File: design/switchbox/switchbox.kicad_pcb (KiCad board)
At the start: 2 copper layers, 59.7 x 29.2 mm, 7 parts, among them J1 A0, J2 GND, SW1 SW_Push, SW2 SW_Push

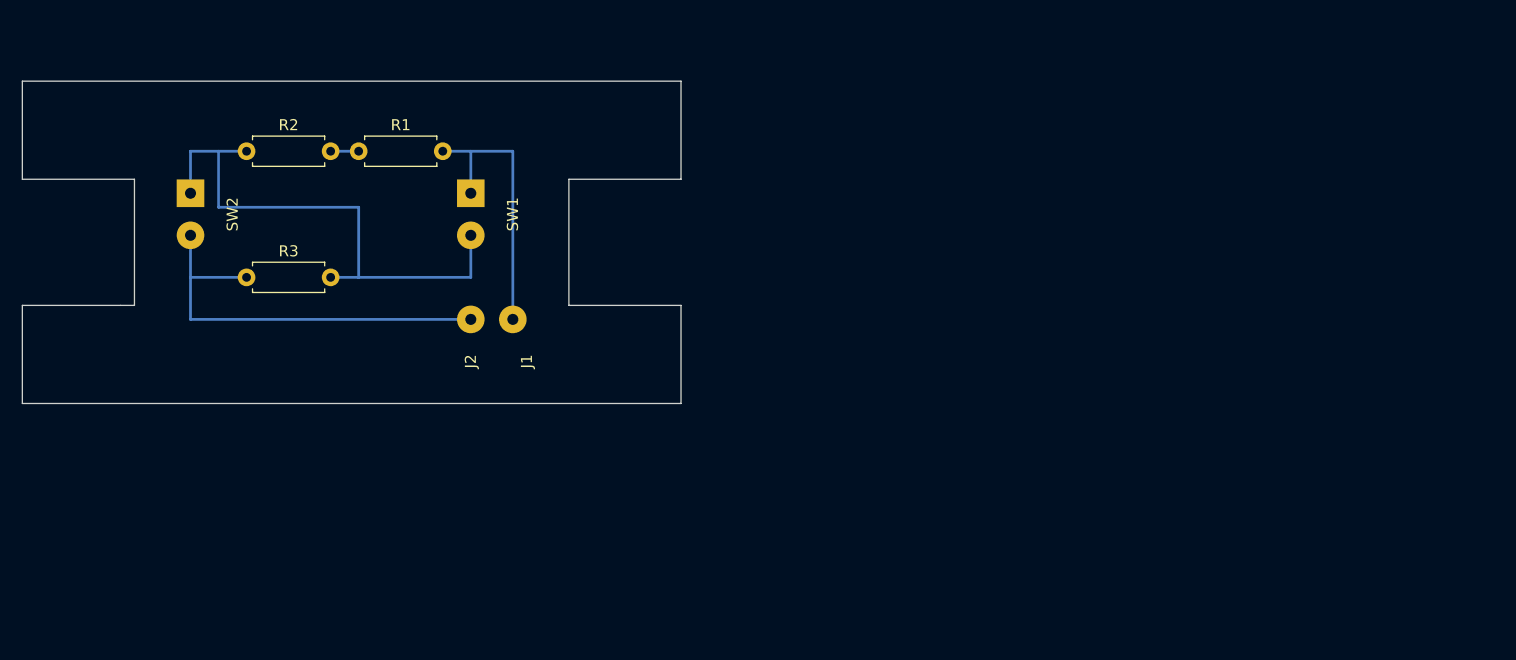
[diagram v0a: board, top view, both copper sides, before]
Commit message: Proper edge cuts alignment
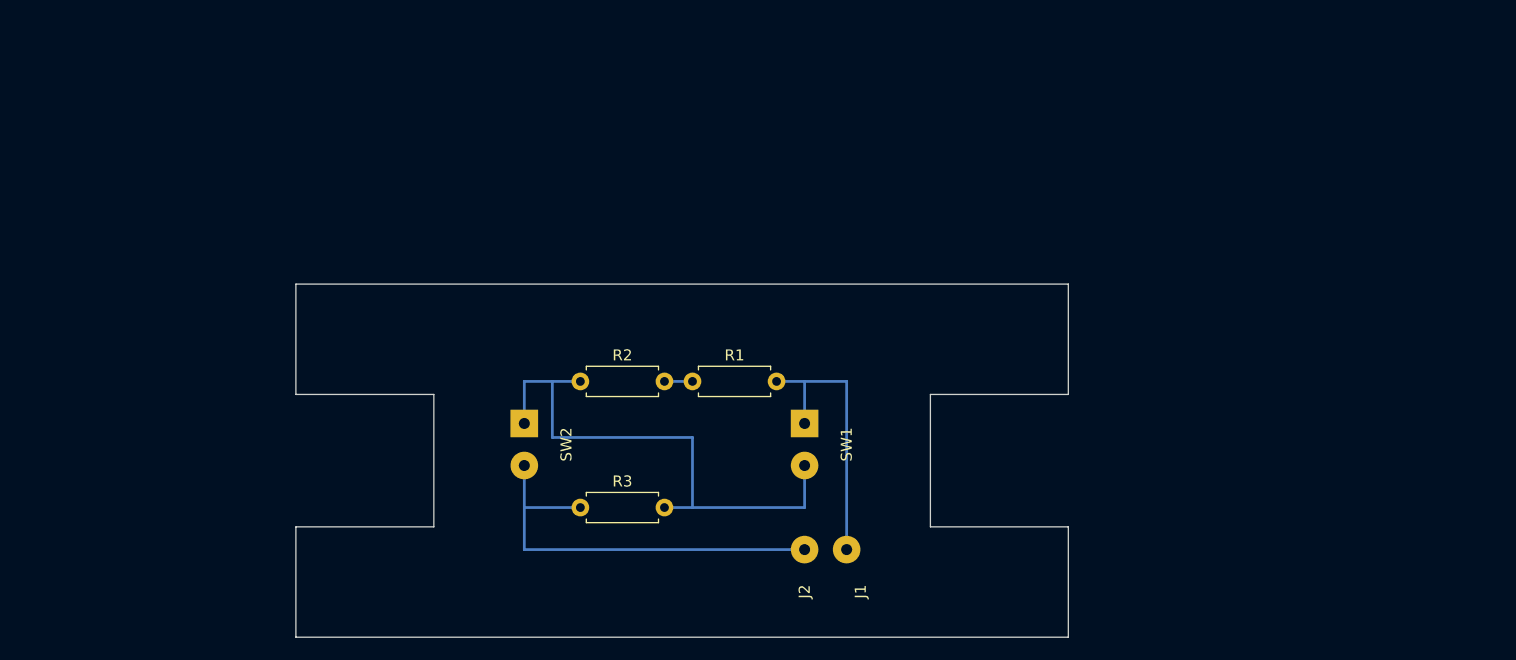
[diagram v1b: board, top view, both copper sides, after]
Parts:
- moved J1 36.7 mm to (167.4, 97.1)
- moved J2 36.7 mm to (163.6, 97.1)
- moved R1 36.7 mm to (153.4, 81.8)
- moved R2 36.7 mm to (143.3, 81.8)
- moved R3 36.7 mm to (143.3, 93.2)
- moved SW1 36.7 mm to (163.6, 85.6)
- moved SW2 36.7 mm to (138.2, 85.6)
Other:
- board size 59.7 x 29.2 mm -> 70 x 32 mm
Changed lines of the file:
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@@
-(kicad_pcb (version 20171130) (host pcbnew 5.1.4+dfsg1-1~bpo10+1)
+(kicad_pcb (version 20171130) (host pcbnew 5.1.5+dfsg1-2~bpo10+1)
   (general
     (thickness 1.6)
-    (drawings 13)
+    (drawings 12)
     (tracks 18)
     (zones 0)
@@
     (35 F.Paste user)
     (36 B.SilkS user)
-    (37 F.SilkS user)
+    (37 F.SilkS user hide)
     (38 B.Mask user)
     (39 F.Mask user)
@@
     (45 Margin user)
     (46 B.CrtYd user)
-    (47 F.CrtYd user)
+    (47 F.CrtYd user hide)
     (48 B.Fab user)
-    (49 F.Fab user)
+    (49 F.Fab user hide)
   )
   (setup
@@
       (outputformat 1)
       (mirror false)
-      (drillshape 1)
+      (drillshape 0)
       (scaleselection 1)
-      (outputdirectory ""))
+      (outputdirectory "gerber"))
   )
   (net 0 "")
@@
   )
   (module Resistor_THT:R_Axial_DIN0207_L6.3mm_D2.5mm_P7.62mm_Horizontal (layer F.Cu)
-    (at 123.19 60.96)
+    (at 153.44 81.82)
     (descr "Resistor, Axial_DIN0207 series, Axial, Horizontal, pin pitch=7.62mm, 0.25W = 1/4W, length*diameter=6.3*2.5mm^2, http://cdn-reichelt.de/documents/datenblatt/B400/1_4W%23YAG.pdf")
     (tags "Resistor Axial_DIN0207 series Axial Horizontal pin pitch 7.62mm 0.25W = 1/4W length 6.3mm diameter 2.5mm")
@@
   )
   (module Resistor_THT:R_Axial_DIN0207_L6.3mm_D2.5mm_P7.62mm_Horizontal (layer F.Cu)
-    (at 113.03 60.96)
+    (at 143.28 81.82)
     (descr "Resistor, Axial_DIN0207 series, Axial, Horizontal, pin pitch=7.62mm, 0.25W = 1/4W, length*diameter=6.3*2.5mm^2, http://cdn-reichelt.de/documents/datenblatt/B400/1_4W%23YAG.pdf")
     (tags "Resistor Axial_DIN0207 series Axial Horizontal pin pitch 7.62mm 0.25W = 1/4W length 6.3mm diameter 2.5mm")
@@
   )
   (module Resistor_THT:R_Axial_DIN0207_L6.3mm_D2.5mm_P7.62mm_Horizontal (layer F.Cu)
-    (at 113.03 72.39)
+    (at 143.28 93.25)
     (descr "Resistor, Axial_DIN0207 series, Axial, Horizontal, pin pitch=7.62mm, 0.25W = 1/4W, length*diameter=6.3*2.5mm^2, http://cdn-reichelt.de/documents/datenblatt/B400/1_4W%23YAG.pdf")
     (tags "Resistor Axial_DIN0207 series Axial Horizontal pin pitch 7.62mm 0.25W = 1/4W length 6.3mm diameter 2.5mm")
@@
   )
   (module Connector_Wire:SolderWirePad_1x02_P3.81mm_Drill1mm (layer F.Cu)
-    (at 133.35 64.77 270)
+    (at 163.6 85.63 270)
     (descr "Wire solder connection")
     (tags connector)
@@
   )
   (module Connector_Wire:SolderWirePad_1x02_P3.81mm_Drill1mm (layer F.Cu)
-    (at 107.95 64.77 270)
+    (at 138.2 85.63 270)
     (descr "Wire solder connection")
     (tags connector)
@@
   )
   (module Connector_Wire:SolderWirePad_1x01_Drill1mm (layer F.Cu)
-    (at 137.16 76.2 90)
+    (at 167.41 97.06 90)
     (descr "Wire solder connection")
     (tags connector)
@@
   )
   (module Connector_Wire:SolderWirePad_1x01_Drill1mm (layer F.Cu)
-    (at 133.35 76.2 90)
+    (at 163.6 97.06 90)
     (descr "Wire solder connection")
     (tags connector)
@@
       (net 4 GND))
   )
-  (gr_line (start 92.71 63.5) (end 92.71 54.61) (layer Edge.Cuts) (width 0.05))
-  (gr_line (start 102.87 63.5) (end 92.71 63.5) (layer Edge.Cuts) (width 0.05))
-  (gr_line (start 102.87 74.93) (end 102.87 63.5) (layer Edge.Cuts) (width 0.05))
-  (gr_line (start 101.6 74.93) (end 102.87 74.93) (layer Edge.Cuts) (width 0.05))
-  (gr_line (start 92.71 74.93) (end 101.6 74.93) (layer Edge.Cuts) (width 0.05))
-  (gr_line (start 92.71 83.82) (end 92.71 74.93) (layer Edge.Cuts) (width 0.05))
-  (gr_line (start 152.4 83.82) (end 92.71 83.82) (layer Edge.Cuts) (width 0.05))
-  (gr_line (start 152.4 74.93) (end 152.4 83.82) (layer Edge.Cuts) (width 0.05))
-  (gr_line (start 142.24 74.93) (end 152.4 74.93) (layer Edge.Cuts) (width 0.05))
-  (gr_line (start 142.24 63.5) (end 142.24 74.93) (layer Edge.Cuts) (width 0.05))
-  (gr_line (start 152.4 63.5) (end 142.24 63.5) (layer Edge.Cuts) (width 0.05))
-  (gr_line (start 152.4 54.61) (end 152.4 63.5) (layer Edge.Cuts) (width 0.05))
-  (gr_line (start 92.71 54.61) (end 152.4 54.61) (layer Edge.Cuts) (width 0.05))
-  (segment (start 120.65 60.96) (end 123.19 60.96) (width 0.25) (layer B.Cu) (net 1))
-  (segment (start 130.81 60.96) (end 133.35 60.96) (width 0.25) (layer B.Cu) (net 2))
-  (segment (start 133.35 60.96) (end 133.35 64.77) (width 0.25) (layer B.Cu) (net 2))
-  (segment (start 133.35 60.96) (end 137.16 60.96) (width 0.25) (layer B.Cu) (net 2))
-  (segment (start 137.16 60.96) (end 137.16 76.2) (width 0.25) (layer B.Cu) (net 2))
-  (segment (start 107.95 60.96) (end 107.95 64.77) (width 0.25) (layer B.Cu) (net 3))
-  (segment (start 110.49 60.96) (end 110.49 66.04) (width 0.25) (layer B.Cu) (net 3))
-  (segment (start 110.49 60.96) (end 107.95 60.96) (width 0.25) (layer B.Cu) (net 3))
-  (segment (start 113.03 60.96) (end 110.49 60.96) (width 0.25) (layer B.Cu) (net 3))
-  (segment (start 110.49 66.04) (end 123.19 66.04) (width 0.25) (layer B.Cu) (net 3))
-  (segment (start 123.19 66.04) (end 123.19 72.39) (width 0.25) (layer B.Cu) (net 3))
-  (segment (start 123.19 72.39) (end 120.65 72.39) (width 0.25) (layer B.Cu) (net 3))
-  (segment (start 123.19 72.39) (end 133.35 72.39) (width 0.25) (layer B.Cu) (net 3))
-  (segment (start 133.35 72.39) (end 133.35 68.58) (width 0.25) (layer B.Cu) (net 3))
-  (segment (start 107.95 68.58) (end 107.95 72.39) (width 0.25) (layer B.Cu) (net 4))
-  (segment (start 107.95 72.39) (end 113.03 72.39) (width 0.25) (layer B.Cu) (net 4))
-  (segment (start 107.95 72.39) (end 107.95 76.2) (width 0.25) (layer B.Cu) (net 4))
-  (segment (start 107.95 76.2) (end 133.35 76.2) (width 0.25) (layer B.Cu) (net 4))
+  (gr_line (start 187.5 105) (end 187.5 95) (layer Edge.Cuts) (width 0.05))
+  (gr_line (start 117.5 105) (end 187.5 105) (layer Edge.Cuts) (width 0.05))
+  (gr_line (start 117.5 95) (end 117.5 105) (layer Edge.Cuts) (width 0.05))
+  (gr_line (start 187.5 73) (end 187.5 83) (layer Edge.Cuts) (width 0.05))
+  (gr_line (start 117.5 73) (end 187.5 73) (layer Edge.Cuts) (width 0.05))
+  (gr_line (start 117.5 83) (end 117.5 73) (layer Edge.Cuts) (width 0.05))
+  (gr_line (start 175 95) (end 187.5 95) (layer Edge.Cuts) (width 0.05))
+  (gr_line (start 175 83) (end 187.5 83) (layer Edge.Cuts) (width 0.05))
+  (gr_line (start 130 83) (end 117.5 83) (layer Edge.Cuts) (width 0.05))
+  (gr_line (start 130 95) (end 117.5 95) (layer Edge.Cuts) (width 0.05))
+  (gr_line (start 175 95) (end 175 83) (layer Edge.Cuts) (width 0.05))
+  (gr_line (start 130 95) (end 130 83) (layer Edge.Cuts) (width 0.05))
+  (segment (start 150.9 81.82) (end 153.44 81.82) (width 0.25) (layer B.Cu) (net 1))
+  (segment (start 161.06 81.82) (end 163.6 81.82) (width 0.25) (layer B.Cu) (net 2))
+  (segment (start 163.6 81.82) (end 163.6 85.63) (width 0.25) (layer B.Cu) (net 2))
+  (segment (start 163.6 81.82) (end 167.41 81.82) (width 0.25) (layer B.Cu) (net 2))
+  (segment (start 167.41 81.82) (end 167.41 97.06) (width 0.25) (layer B.Cu) (net 2))
+  (segment (start 138.2 81.82) (end 138.2 85.63) (width 0.25) (layer B.Cu) (net 3))
+  (segment (start 140.74 81.82) (end 140.74 86.9) (width 0.25) (layer B.Cu) (net 3))
+  (segment (start 140.74 81.82) (end 138.2 81.82) (width 0.25) (layer B.Cu) (net 3))
+  (segment (start 143.28 81.82) (end 140.74 81.82) (width 0.25) (layer B.Cu) (net 3))
+  (segment (start 140.74 86.9) (end 153.44 86.9) (width 0.25) (layer B.Cu) (net 3))
+  (segment (start 153.44 86.9) (end 153.44 93.25) (width 0.25) (layer B.Cu) (net 3))
+  (segment (start 153.44 93.25) (end 150.9 93.25) (width 0.25) (layer B.Cu) (net 3))
+  (segment (start 153.44 93.25) (end 163.6 93.25) (width 0.25) (layer B.Cu) (net 3))
+  (segment (start 163.6 93.25) (end 163.6 89.44) (width 0.25) (layer B.Cu) (net 3))
+  (segment (start 138.2 89.44) (end 138.2 93.25) (width 0.25) (layer B.Cu) (net 4))
+  (segment (start 138.2 93.25) (end 143.28 93.25) (width 0.25) (layer B.Cu) (net 4))
+  (segment (start 138.2 93.25) (end 138.2 97.06) (width 0.25) (layer B.Cu) (net 4))
+  (segment (start 138.2 97.06) (end 163.6 97.06) (width 0.25) (layer B.Cu) (net 4))
 )

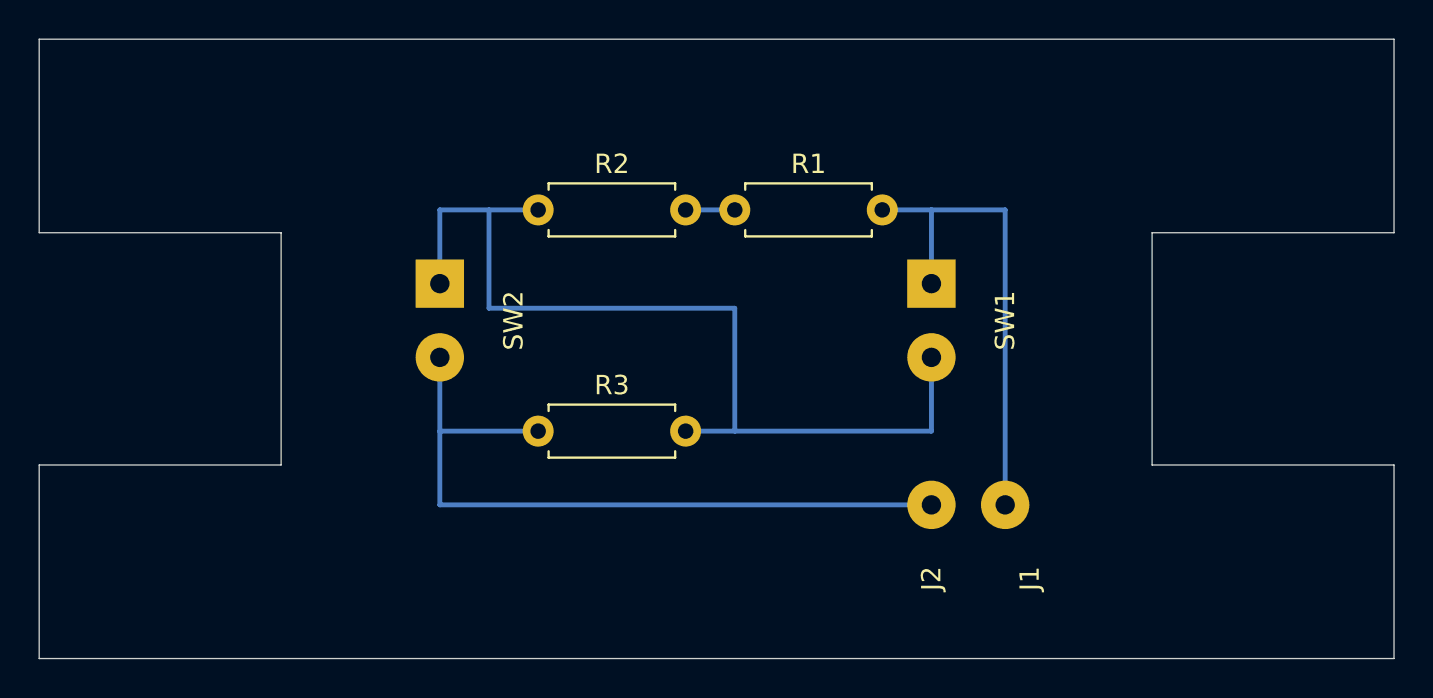
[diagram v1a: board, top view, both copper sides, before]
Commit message: Added filled areas
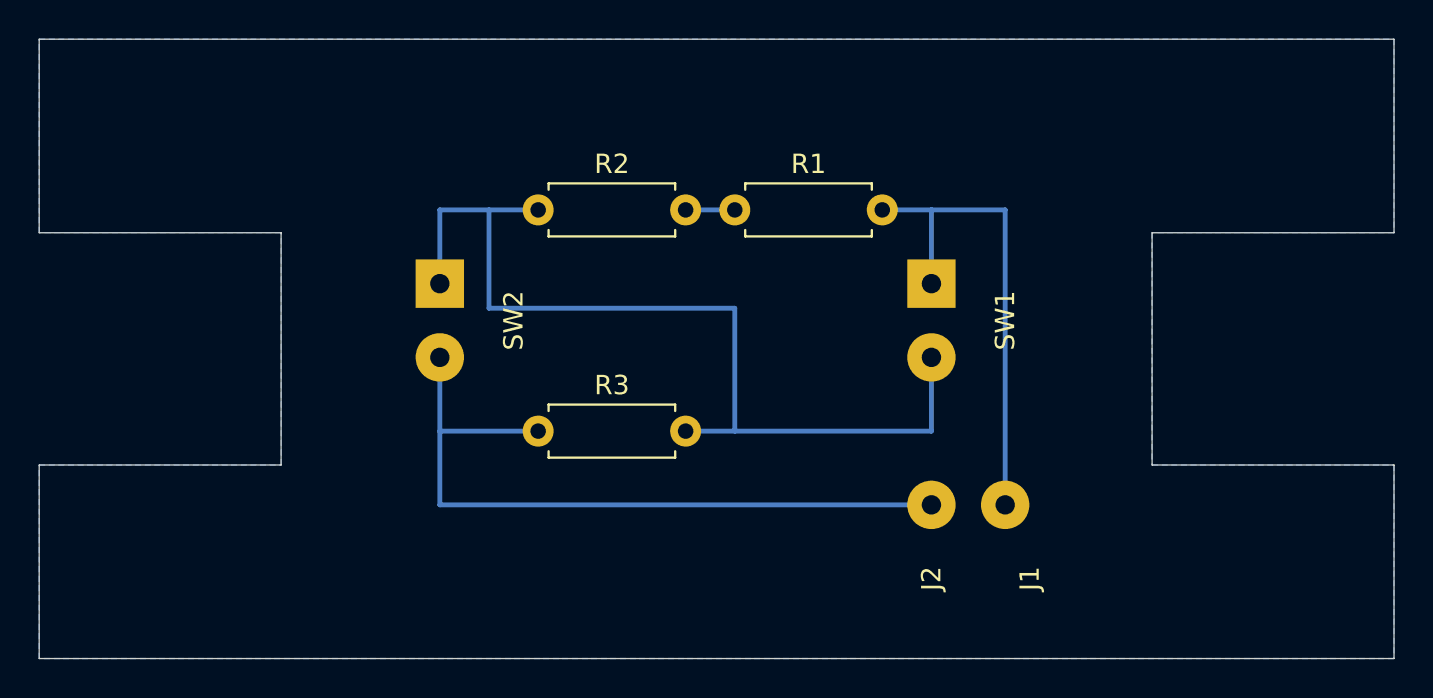
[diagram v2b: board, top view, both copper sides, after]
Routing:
- added copper zone on B.Cu, net (none)
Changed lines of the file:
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@@
   (segment (start 138.2 93.25) (end 138.2 97.06) (width 0.25) (layer B.Cu) (net 4))
   (segment (start 138.2 97.06) (end 163.6 97.06) (width 0.25) (layer B.Cu) (net 4))
+  (zone (net 0) (net_name "") (layer B.Cu) (hatch edge 0.508)
+    (connect_pads (clearance 0.508))
+    (min_thickness 0.254)
+    (fill yes (arc_segments 32) (thermal_gap 0.508) (thermal_bridge_width 0.508))
+    (polygon
+      (pts
+        (xy 187.5 83) (xy 175 83) (xy 175 95) (xy 187.5 95) (xy 187.5 105)
+        (xy 117.5 105) (xy 117.5 95) (xy 130 95) (xy 130 83) (xy 117.5 83)
+        (xy 117.5 73) (xy 187.5 73)
+      )
+    )
+  )
 )

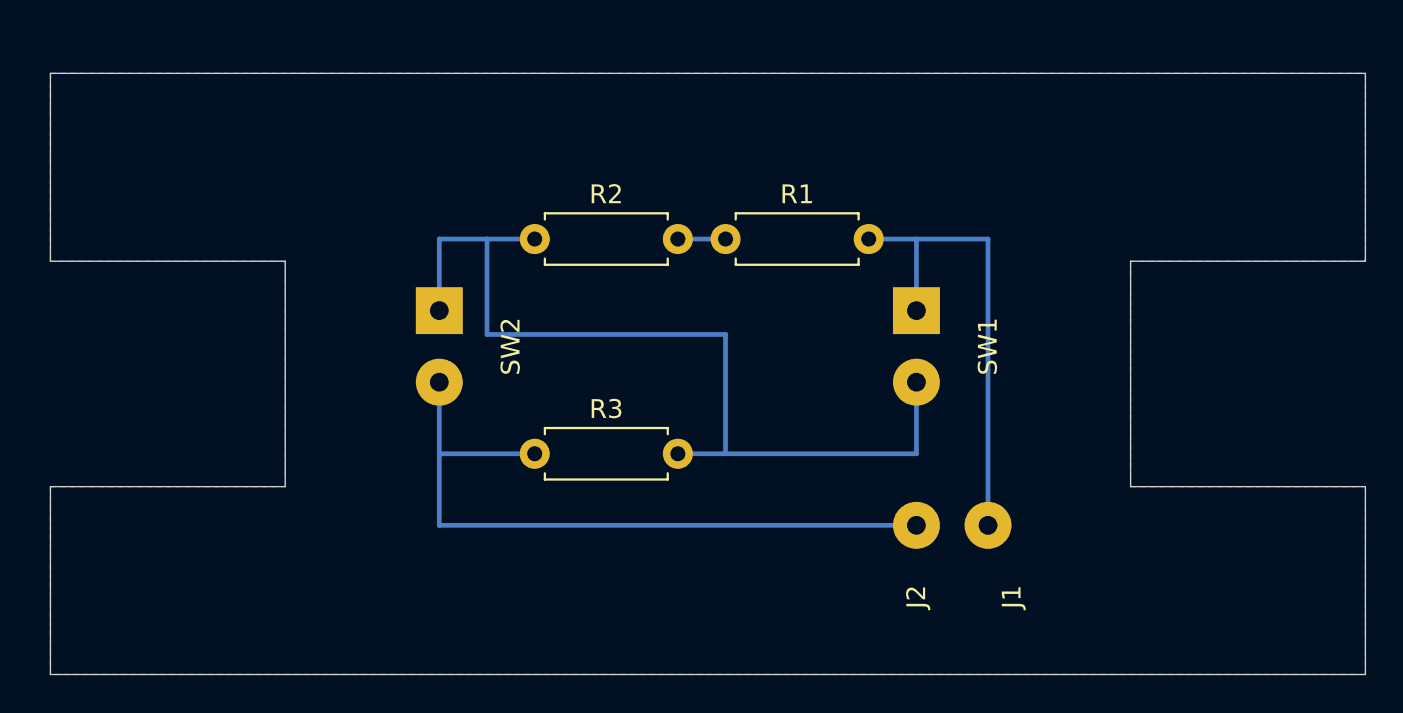
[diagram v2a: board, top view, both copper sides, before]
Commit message: Updated footprints for wire connectors, angles on tracks changed to 45 degrees
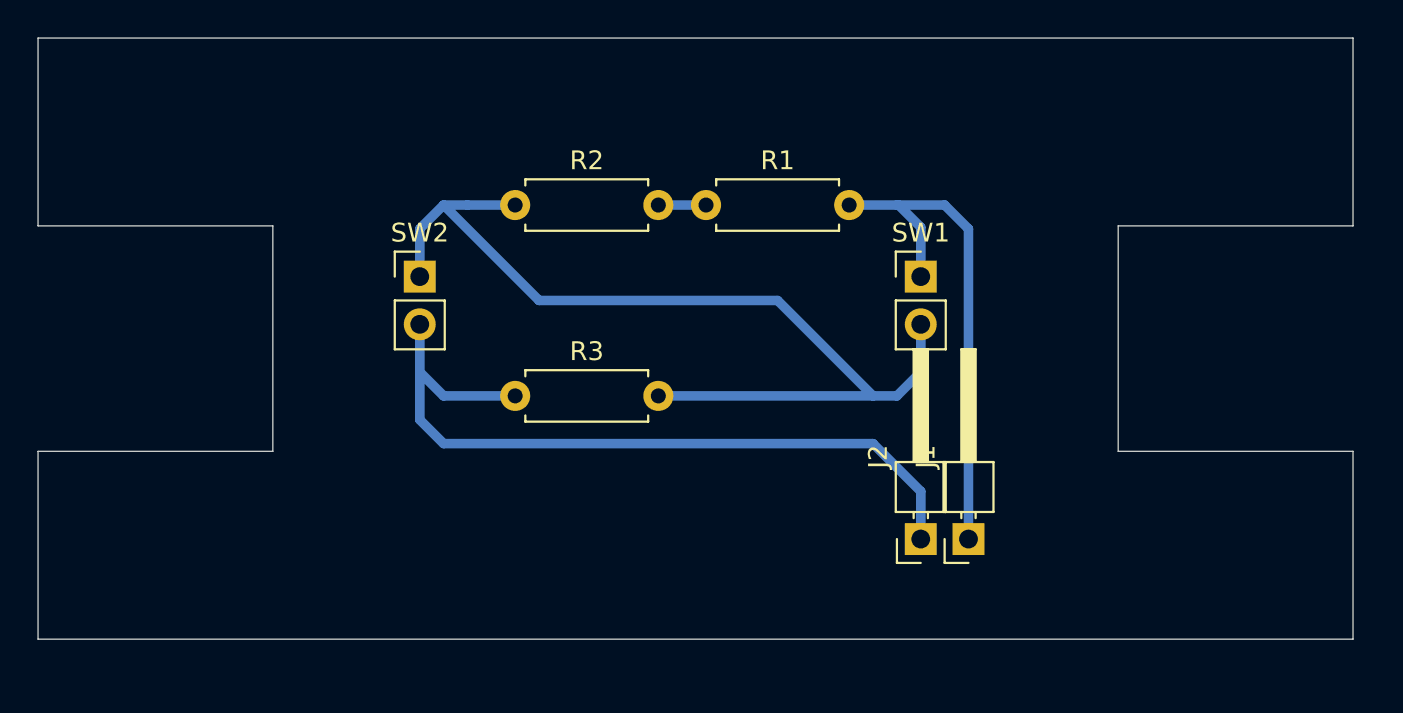
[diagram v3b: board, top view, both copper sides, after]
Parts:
- J1, J2: footprint Connector_Wire:SolderWirePad_1x01_Drill1mm -> Connector_PinHeader_2.54mm:PinHeader_1x01_P2.54mm_Horizontal
- SW1, SW2: footprint Connector_Wire:SolderWirePad_1x02_P3.81mm_Drill1mm -> Connector_PinHeader_2.54mm:PinHeader_1x02_P2.54mm_Vertical
- moved R3 3.25 mm to (142.2, 90.2)
- moved SW2 2.09 mm to (137.2, 83.8), turned to 0 degrees
- moved R1 2.09 mm to (152.4, 80.0)
- moved R2 2.09 mm to (142.2, 80.0)
- moved SW1 1.82 mm to (163.8, 83.8), turned to 0 degrees
- moved J1 1.27 mm to (166.4, 97.8)
- moved J2 0.77 mm to (163.8, 97.8)
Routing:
- net GND: track 38.1 -> 41.5 mm
- net Net-(R2-Pad1): track 49.5 -> 52.3 mm
- net +5V: track 25.4 -> 27.7 mm
- removed copper zone on B.Cu, net (none)
